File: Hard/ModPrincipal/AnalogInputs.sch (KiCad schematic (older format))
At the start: 15 parts, among them U201 LM324

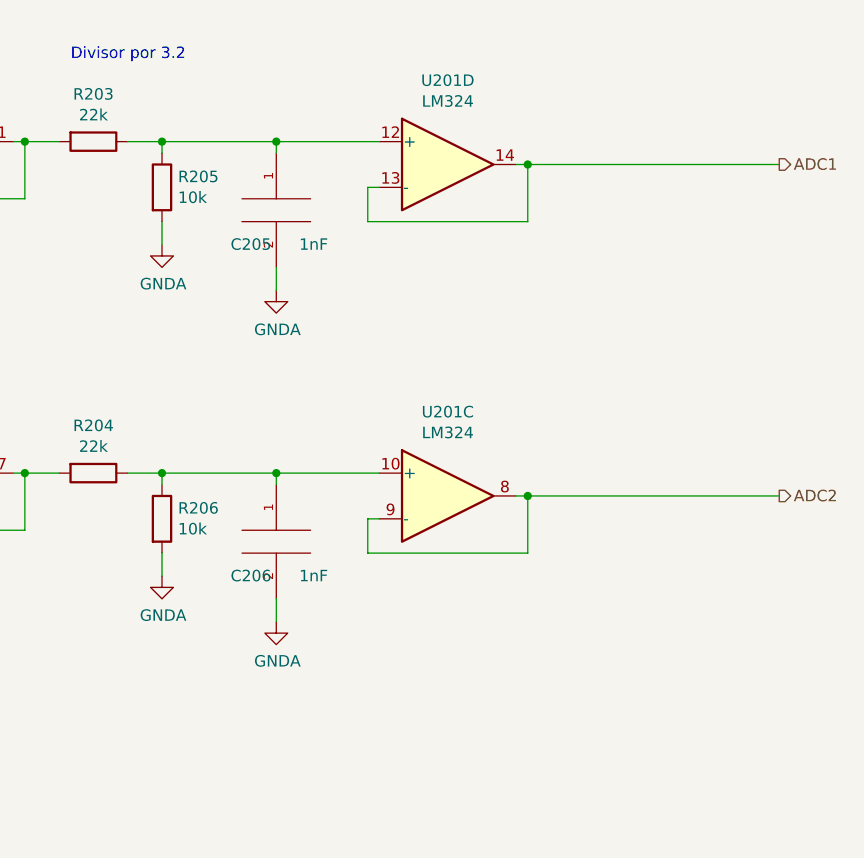
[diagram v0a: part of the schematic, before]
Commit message: Agrego UART aislada y salidas digitales
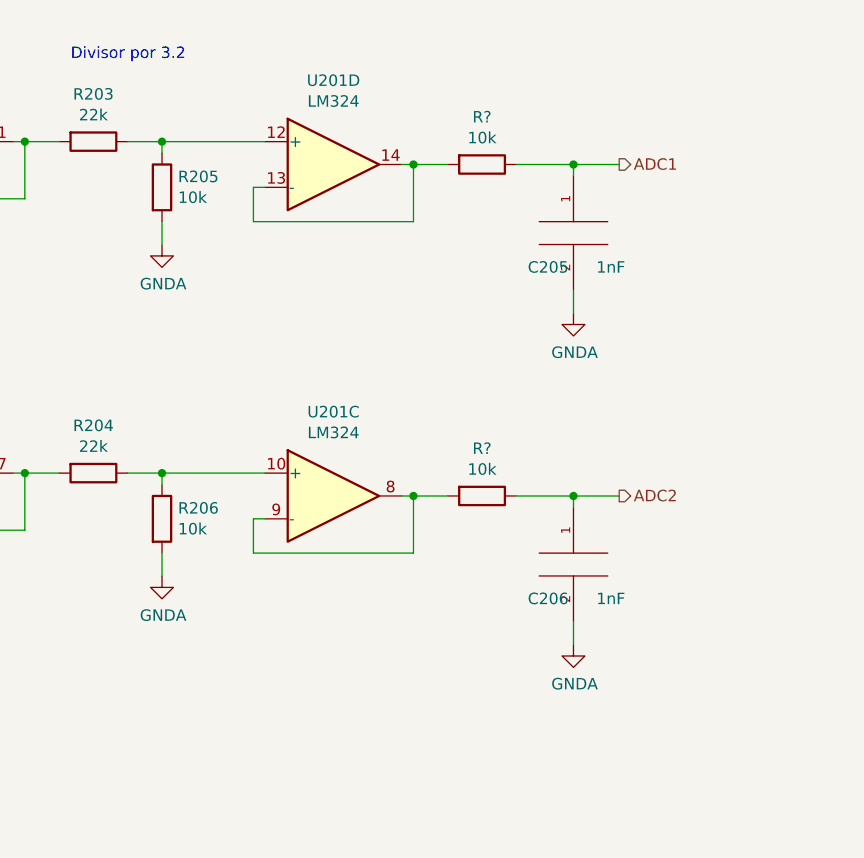
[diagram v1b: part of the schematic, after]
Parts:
- added R? (x2): 10k, Resistor_SMD:R_0805_2012Metric_Pad1.15x1.40mm_HandSolder, symbol Device:R
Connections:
- net ADC1: now also C205.1, R?.1; no longer U201.13 (-), U201.14
- net ADC2: now also C206.1, R?.1; no longer U201.8, U201.9 (-)
- net at R204.1, R206.1, U201.10 (+): no longer C206.1
- net at R203.1, R205.1, U201.12 (+): no longer C205.1
- new net: R?.2, U201.8, U201.9 (-)
- new net: R?.2, U201.13 (-), U201.14
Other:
- moved on the sheet: C205, C206, U201C, U201D
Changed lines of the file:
@@
 EESchema Schematic File Version 4
-LIBS:ModPrincipal-cache
 EELAYER 30 0
 EELAYER END
 $Descr A4 11693 8268
 encoding utf-8
-Sheet 2 4
+Sheet 2 5
 Title ""
 Date ""
@@
 L Amplifier_Operational:LM324 U201
 U 3 1 5EC75219
-P 7350 3600
-F 0 "U201" H 7350 3967 50  0000 C CNN
-F 1 "LM324" H 7350 3876 50  0000 C CNN
-F 2 "" H 7300 3700 50  0001 C CNN
-F 3 "http://www.ti.com/lit/ds/symlink/lm2902-n.pdf" H 7400 3800 50  0001 C CNN
-	3    7350 3600
+P 6850 3600
+F 0 "U201" H 6850 3967 50  0000 C CNN
+F 1 "LM324" H 6850 3876 50  0000 C CNN
+F 2 "" H 6800 3700 50  0001 C CNN
+F 3 "http://www.ti.com/lit/ds/symlink/lm2902-n.pdf" H 6900 3800 50  0001 C CNN
+	3    6850 3600
 	1    0    0    -1
 $EndComp
@@
 L Amplifier_Operational:LM324 U201
 U 4 1 5EC763BC
-P 7350 2150
-F 0 "U201" H 7350 2517 50  0000 C CNN
-F 1 "LM324" H 7350 2426 50  0000 C CNN
-F 2 "" H 7300 2250 50  0001 C CNN
-F 3 "http://www.ti.com/lit/ds/symlink/lm2902-n.pdf" H 7400 2350 50  0001 C CNN
-	4    7350 2150
+P 6850 2150
+F 0 "U201" H 6850 2517 50  0000 C CNN
+F 1 "LM324" H 6850 2426 50  0000 C CNN
+F 2 "" H 6800 2250 50  0001 C CNN
+F 3 "http://www.ti.com/lit/ds/symlink/lm2902-n.pdf" H 6900 2350 50  0001 C CNN
+	4    6850 2150
 	1    0    0    -1
 $EndComp
@@
 	5500 2050 5450 2050
 Wire Wire Line
-	7050 3700 7000 3700
-Wire Wire Line
-	7000 3700 7000 3850
-Wire Wire Line
-	7000 3850 7700 3850
-Wire Wire Line
-	7700 3850 7700 3600
-Wire Wire Line
-	7700 3600 7650 3600
+	6550 3700 6500 3700
+Wire Wire Line
+	6500 3700 6500 3850
+Wire Wire Line
+	6500 3850 7200 3850
+Wire Wire Line
+	7200 3850 7200 3600
+Wire Wire Line
+	7200 3600 7150 3600
 Wire Wire Line
 	4850 3600 4800 3600
@@
 	5500 3500 5450 3500
 Wire Wire Line
-	7050 2250 7000 2250
-Wire Wire Line
-	7000 2400 7700 2400
-Wire Wire Line
-	7700 2150 7650 2150
+	6550 2250 6500 2250
+Wire Wire Line
+	6500 2400 7200 2400
+Wire Wire Line
+	7200 2150 7150 2150
 Wire Wire Line
 	4850 1950 4300 1950
@@
 L pspice:C C205
 U 1 1 5ECFBDEC
-P 6600 2350
-F 0 "C205" H 6400 2200 50  0000 L CNN
-F 1 "1nF" H 6700 2200 50  0000 L CNN
-F 2 "Capacitor_SMD:C_0805_2012Metric_Pad1.15x1.40mm_HandSolder" H 6600 2350 50  0001 C CNN
-F 3 "~" H 6600 2350 50  0001 C CNN
-	1    6600 2350
+P 7900 2450
+F 0 "C205" H 7700 2300 50  0000 L CNN
+F 1 "1nF" H 8000 2300 50  0000 L CNN
+F 2 "Capacitor_SMD:C_0805_2012Metric_Pad1.15x1.40mm_HandSolder" H 7900 2450 50  0001 C CNN
+F 3 "~" H 7900 2450 50  0001 C CNN
+	1    7900 2450
 	1    0    0    -1
 $EndComp
@@
 L power:GNDA #PWR0211
 U 1 1 5ECFBDF2
-P 6600 2700
-F 0 "#PWR0211" H 6600 2450 50  0001 C CNN
-F 1 "GNDA" H 6605 2527 50  0000 C CNN
-F 2 "" H 6600 2700 50  0001 C CNN
-F 3 "" H 6600 2700 50  0001 C CNN
-	1    6600 2700
-	1    0    0    -1
-$EndComp
-Wire Wire Line
-	6600 2600 6600 2700
-Wire Wire Line
-	7000 2250 7000 2400
-Wire Wire Line
-	7050 2050 6600 2050
-Connection ~ 6100 2050
-Wire Wire Line
-	6600 2100 6600 2050
-Connection ~ 6600 2050
-Wire Wire Line
-	6600 2050 6100 2050
+P 7900 2800
+F 0 "#PWR0211" H 7900 2550 50  0001 C CNN
+F 1 "GNDA" H 7905 2627 50  0000 C CNN
+F 2 "" H 7900 2800 50  0001 C CNN
+F 3 "" H 7900 2800 50  0001 C CNN
+	1    7900 2800
+	1    0    0    -1
+$EndComp
+Wire Wire Line
+	7900 2700 7900 2800
+Wire Wire Line
+	6500 2250 6500 2400
+Wire Wire Line
+	7900 2200 7900 2150
 $Comp
 L pspice:C C206
 U 1 1 5ED294AB
-P 6600 3800
-F 0 "C206" H 6400 3650 50  0000 L CNN
-F 1 "1nF" H 6700 3650 50  0000 L CNN
-F 2 "Capacitor_SMD:C_0805_2012Metric_Pad1.15x1.40mm_HandSolder" H 6600 3800 50  0001 C CNN
-F 3 "~" H 6600 3800 50  0001 C CNN
-	1    6600 3800
+P 7900 3900
+F 0 "C206" H 7700 3750 50  0000 L CNN
+F 1 "1nF" H 8000 3750 50  0000 L CNN
+F 2 "Capacitor_SMD:C_0805_2012Metric_Pad1.15x1.40mm_HandSolder" H 7900 3900 50  0001 C CNN
+F 3 "~" H 7900 3900 50  0001 C CNN
+	1    7900 3900
 	1    0    0    -1
 $EndComp
@@
 L power:GNDA #PWR0212
 U 1 1 5ED294B1
-P 6600 4150
-F 0 "#PWR0212" H 6600 3900 50  0001 C CNN
-F 1 "GNDA" H 6605 3977 50  0000 C CNN
-F 2 "" H 6600 4150 50  0001 C CNN
-F 3 "" H 6600 4150 50  0001 C CNN
-	1    6600 4150
-	1    0    0    -1
-$EndComp
-Wire Wire Line
-	6600 4050 6600 4150
-Wire Wire Line
-	7050 3500 6600 3500
-Connection ~ 6100 3500
-Wire Wire Line
-	6600 3550 6600 3500
-Connection ~ 6600 3500
-Wire Wire Line
-	6600 3500 6100 3500
-Text HLabel 8800 2150 2    50   Output ~ 0
+P 7900 4250
+F 0 "#PWR0212" H 7900 4000 50  0001 C CNN
+F 1 "GNDA" H 7905 4077 50  0000 C CNN
+F 2 "" H 7900 4250 50  0001 C CNN
+F 3 "" H 7900 4250 50  0001 C CNN
+	1    7900 4250
+	1    0    0    -1
+$EndComp
+Wire Wire Line
+	7900 4150 7900 4250
+Wire Wire Line
+	7900 3650 7900 3600
+Text HLabel 8100 2150 2    50   Output ~ 0
 ADC1
-Text HLabel 8800 3600 2    50   Output ~ 0
+Text HLabel 8100 3600 2    50   Output ~ 0
 ADC2
 Wire Wire Line
-	7700 2400 7700 2150
-Wire Wire Line
-	8800 2150 7700 2150
-Connection ~ 7700 2150
-Wire Wire Line
-	8800 3600 7700 3600
-Connection ~ 7700 3600
+	7200 2400 7200 2150
+Wire Wire Line
+	8100 2150 7900 2150
+Wire Wire Line
+	8100 3600 7900 3600
 $Comp
 L power:GNDA #PWR0204
@@
 	2050 5800 2050 5850
 Connection ~ 2050 5850
+$Comp
+L Device:R R?
+U 1 1 5ED0C39C
+P 7500 2150
+F 0 "R?" V 7293 2150 50  0000 C CNN
+F 1 "10k" V 7384 2150 50  0000 C CNN
+F 2 "Resistor_SMD:R_0805_2012Metric_Pad1.15x1.40mm_HandSolder" V 7430 2150 50  0001 C CNN
+F 3 "~" H 7500 2150 50  0001 C CNN
+	1    7500 2150
+	0    1    1    0
+$EndComp
+$Comp
+L Device:R R?
+U 1 1 5ED0D996
+P 7500 3600
+F 0 "R?" V 7293 3600 50  0000 C CNN
+F 1 "10k" V 7384 3600 50  0000 C CNN
+F 2 "Resistor_SMD:R_0805_2012Metric_Pad1.15x1.40mm_HandSolder" V 7430 3600 50  0001 C CNN
+F 3 "~" H 7500 3600 50  0001 C CNN
+	1    7500 3600
+	0    1    1    0
+$EndComp
+Wire Wire Line
+	7650 3600 7900 3600
+Connection ~ 7900 3600
+Wire Wire Line
+	7350 3600 7200 3600
+Connection ~ 7200 3600
+Wire Wire Line
+	7900 2150 7650 2150
+Connection ~ 7900 2150
+Wire Wire Line
+	7200 2150 7350 2150
+Connection ~ 7200 2150
+Wire Wire Line
+	6550 2050 6100 2050
+Connection ~ 6100 2050
+Wire Wire Line
+	6100 3500 6550 3500
+Connection ~ 6100 3500
 $EndSCHEMATC

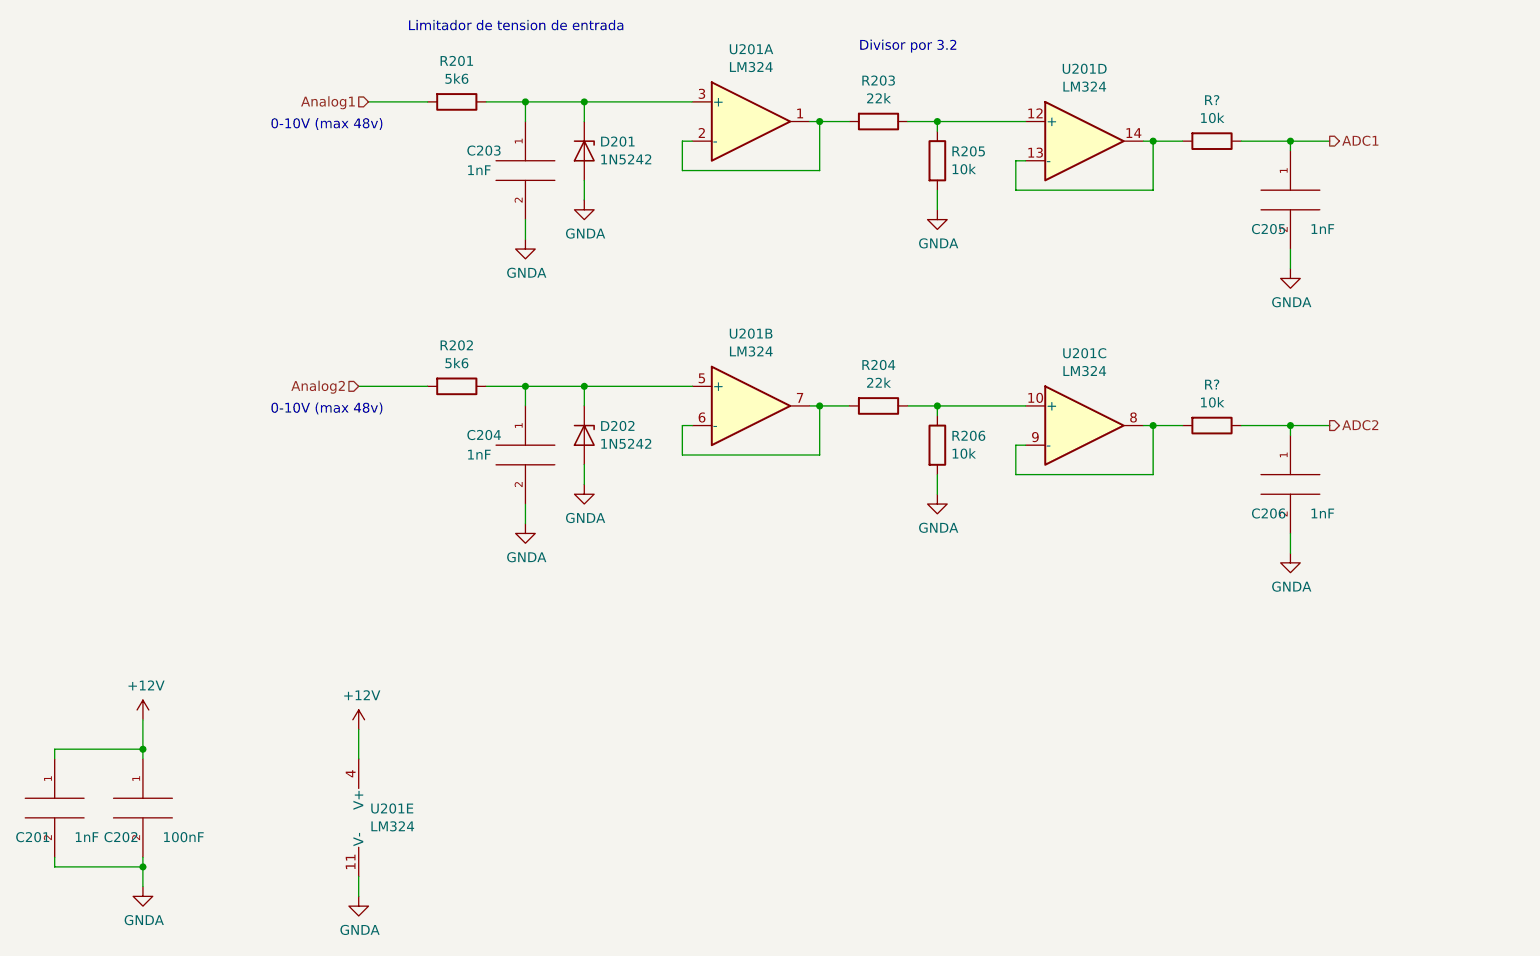
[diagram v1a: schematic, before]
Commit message: Agrego fuente de alimentación
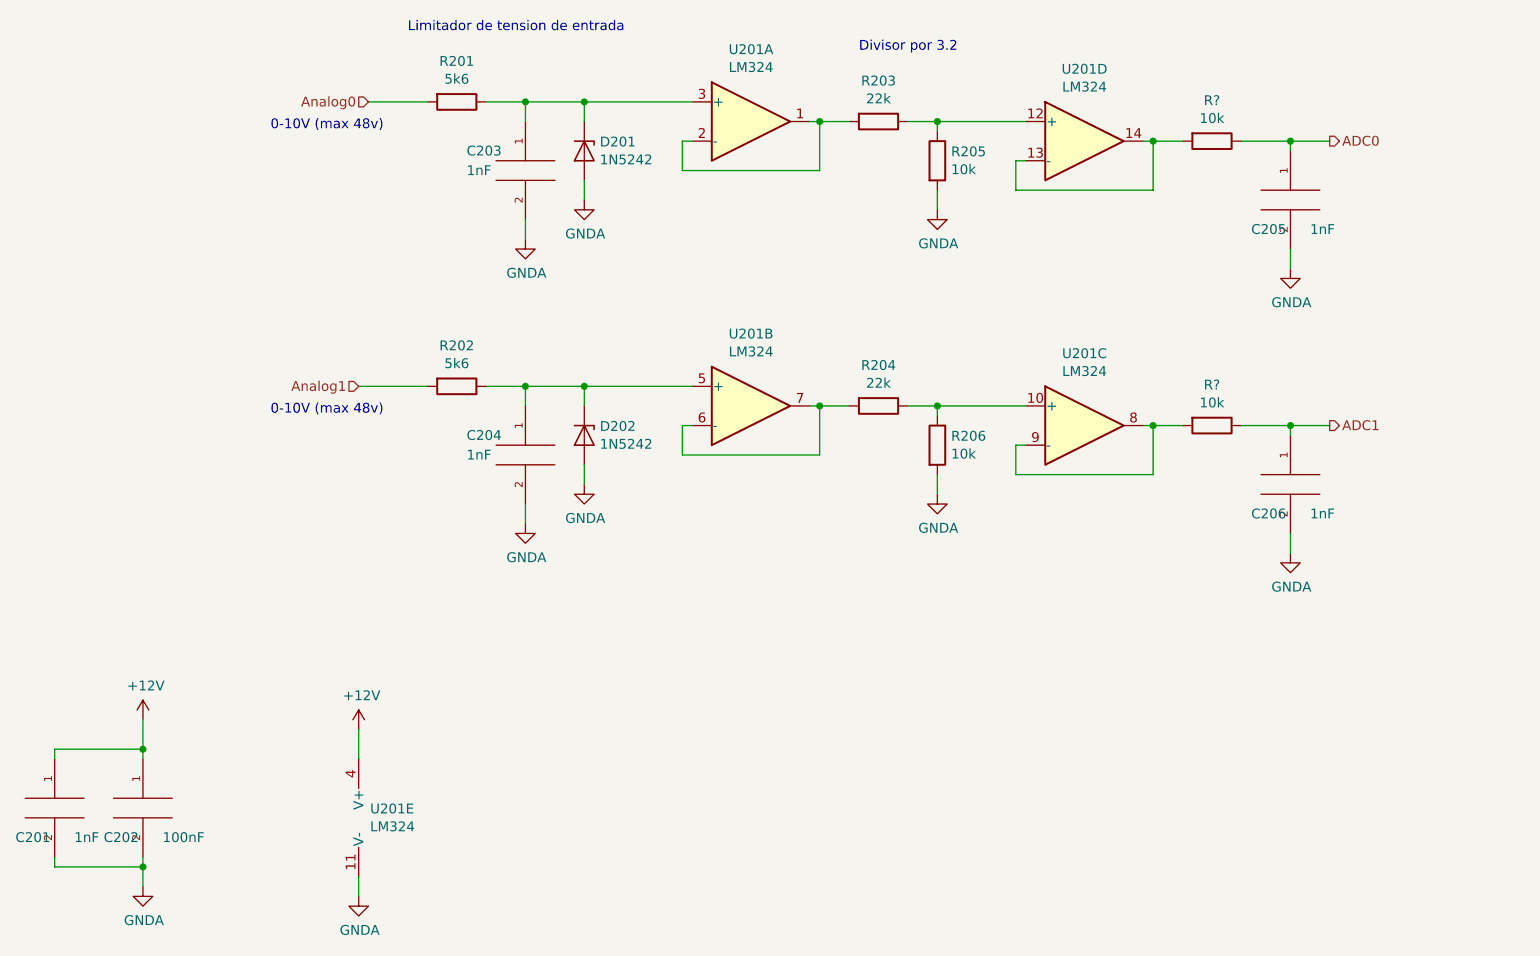
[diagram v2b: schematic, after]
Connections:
- net ADC2 is gone; now on net ADC1: C206.1, R?.1
- net Analog2 is gone; now on net Analog1: R202.2
- net ADC1: no longer C205.1, R?.1
- net Analog1: no longer R201.2
- new net ADC0: C205.1, R?.1
- new net Analog0: R201.2
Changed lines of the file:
@@
 $Descr A4 11693 8268
 encoding utf-8
-Sheet 2 5
+Sheet 2 8
 Title ""
 Date ""
@@
 	4000 1950 4300 1950
 Text HLabel 3200 1950 0    50   Input ~ 0
+Analog0
+Text HLabel 3150 3400 0    50   Input ~ 0
 Analog1
-Text HLabel 3150 3400 0    50   Input ~ 0
-Analog2
 $Comp
 L Device:R R202
@@
 	7900 3650 7900 3600
 Text HLabel 8100 2150 2    50   Output ~ 0
+ADC0
+Text HLabel 8100 3600 2    50   Output ~ 0
 ADC1
-Text HLabel 8100 3600 2    50   Output ~ 0
-ADC2
 Wire Wire Line
 	7200 2400 7200 2150

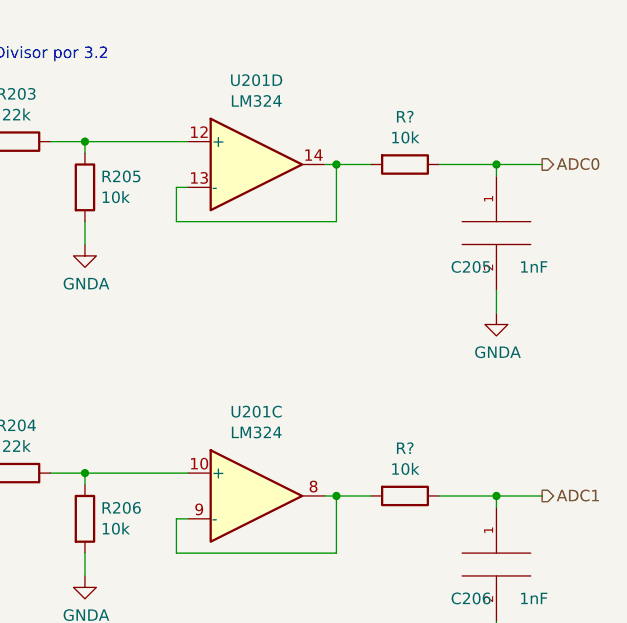
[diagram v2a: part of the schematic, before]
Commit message: Asignacion inicial de footprints
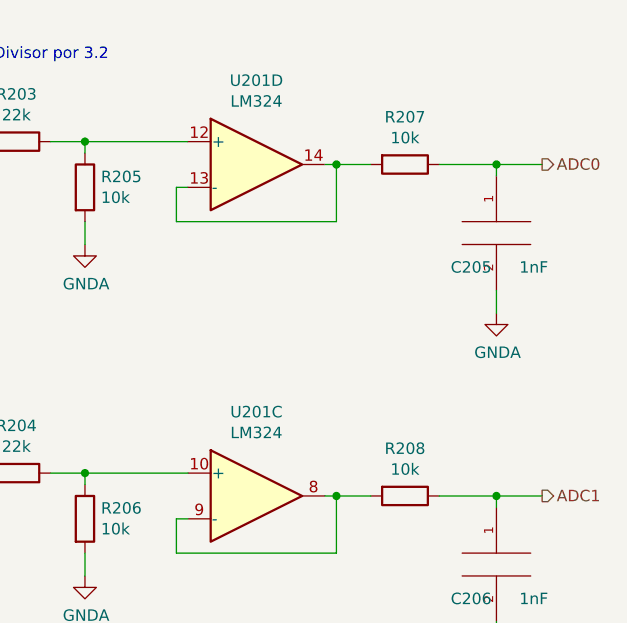
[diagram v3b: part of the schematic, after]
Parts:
- U201: footprint (none) -> Package_SO:SOIC-14_3.9x8.7mm_P1.27mm
- gave numbers to parts that had none: 2
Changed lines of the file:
@@
 EESchema Schematic File Version 4
+LIBS:ModPrincipal-cache
 EELAYER 30 0
 EELAYER END
@@
 F 0 "U201" H 5150 2417 50  0000 C CNN
 F 1 "LM324" H 5150 2326 50  0000 C CNN
-F 2 "" H 5100 2150 50  0001 C CNN
+F 2 "Package_SO:SOIC-14_3.9x8.7mm_P1.27mm" H 5100 2150 50  0001 C CNN
 F 3 "http://www.ti.com/lit/ds/symlink/lm2902-n.pdf" H 5200 2250 50  0001 C CNN
 	1    5150 2050
@@
 F 0 "U201" H 5150 3867 50  0000 C CNN
 F 1 "LM324" H 5150 3776 50  0000 C CNN
-F 2 "" H 5100 3600 50  0001 C CNN
+F 2 "Package_SO:SOIC-14_3.9x8.7mm_P1.27mm" H 5100 3600 50  0001 C CNN
 F 3 "http://www.ti.com/lit/ds/symlink/lm2902-n.pdf" H 5200 3700 50  0001 C CNN
 	2    5150 3500
@@
 F 0 "U201" H 6850 3967 50  0000 C CNN
 F 1 "LM324" H 6850 3876 50  0000 C CNN
-F 2 "" H 6800 3700 50  0001 C CNN
+F 2 "Package_SO:SOIC-14_3.9x8.7mm_P1.27mm" H 6800 3700 50  0001 C CNN
 F 3 "http://www.ti.com/lit/ds/symlink/lm2902-n.pdf" H 6900 3800 50  0001 C CNN
 	3    6850 3600
@@
 F 0 "U201" H 6850 2517 50  0000 C CNN
 F 1 "LM324" H 6850 2426 50  0000 C CNN
-F 2 "" H 6800 2250 50  0001 C CNN
+F 2 "Package_SO:SOIC-14_3.9x8.7mm_P1.27mm" H 6800 2250 50  0001 C CNN
 F 3 "http://www.ti.com/lit/ds/symlink/lm2902-n.pdf" H 6900 2350 50  0001 C CNN
 	4    6850 2150
@@
 F 0 "U201" H 3208 5646 50  0000 L CNN
 F 1 "LM324" H 3208 5555 50  0000 L CNN
-F 2 "" H 3200 5700 50  0001 C CNN
+F 2 "Package_SO:SOIC-14_3.9x8.7mm_P1.27mm" H 3200 5700 50  0001 C CNN
 F 3 "http://www.ti.com/lit/ds/symlink/lm2902-n.pdf" H 3300 5800 50  0001 C CNN
 	5    3250 5600
@@
 Connection ~ 2050 5850
 $Comp
-L Device:R R?
+L Device:R R207
 U 1 1 5ED0C39C
 P 7500 2150
-F 0 "R?" V 7293 2150 50  0000 C CNN
+F 0 "R207" V 7293 2150 50  0000 C CNN
 F 1 "10k" V 7384 2150 50  0000 C CNN
 F 2 "Resistor_SMD:R_0805_2012Metric_Pad1.15x1.40mm_HandSolder" V 7430 2150 50  0001 C CNN
@@
 $EndComp
 $Comp
-L Device:R R?
+L Device:R R208
 U 1 1 5ED0D996
 P 7500 3600
-F 0 "R?" V 7293 3600 50  0000 C CNN
+F 0 "R208" V 7293 3600 50  0000 C CNN
 F 1 "10k" V 7384 3600 50  0000 C CNN
 F 2 "Resistor_SMD:R_0805_2012Metric_Pad1.15x1.40mm_HandSolder" V 7430 3600 50  0001 C CNN
